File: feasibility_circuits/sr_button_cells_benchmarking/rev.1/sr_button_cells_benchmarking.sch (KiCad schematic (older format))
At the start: 48 parts, among them J1 Current Measurement, J10 Jumper, J11 EN_MED_CURR, J12 Jumper, J2 EN_POT, J3 GND, J4 GND, J5 Jumper, J6 VIN, J7 EN_HIGH_CURR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

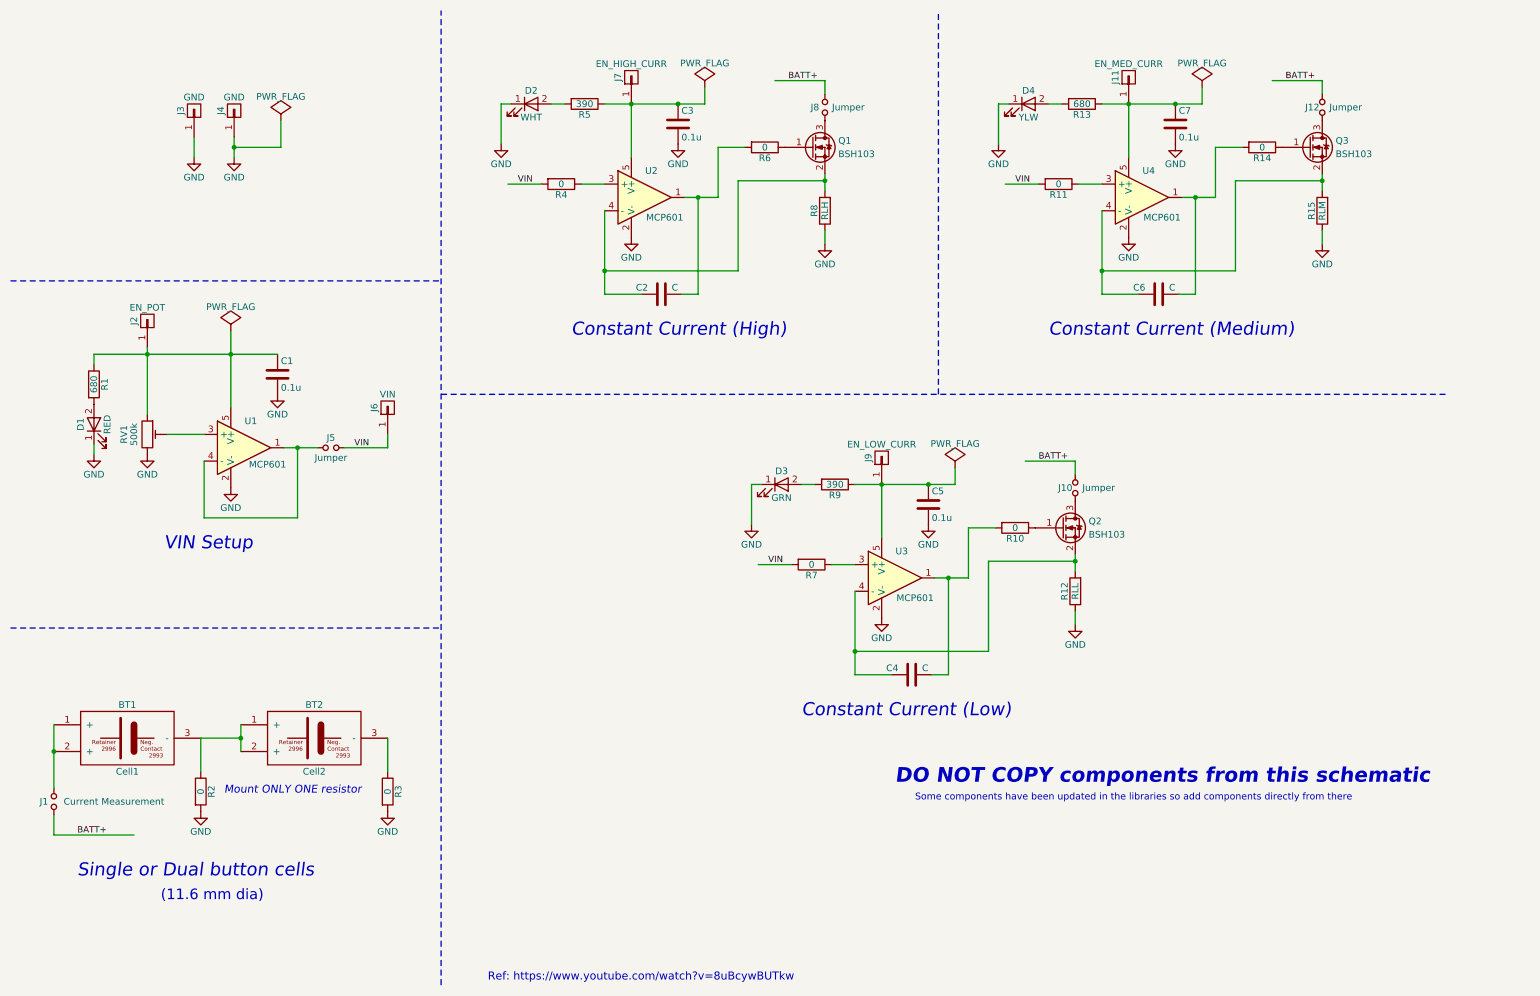
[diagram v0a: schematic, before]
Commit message: Review and organisation
Review of Auxiliary PIC and IR barrier setup board. Organisation of
resources.
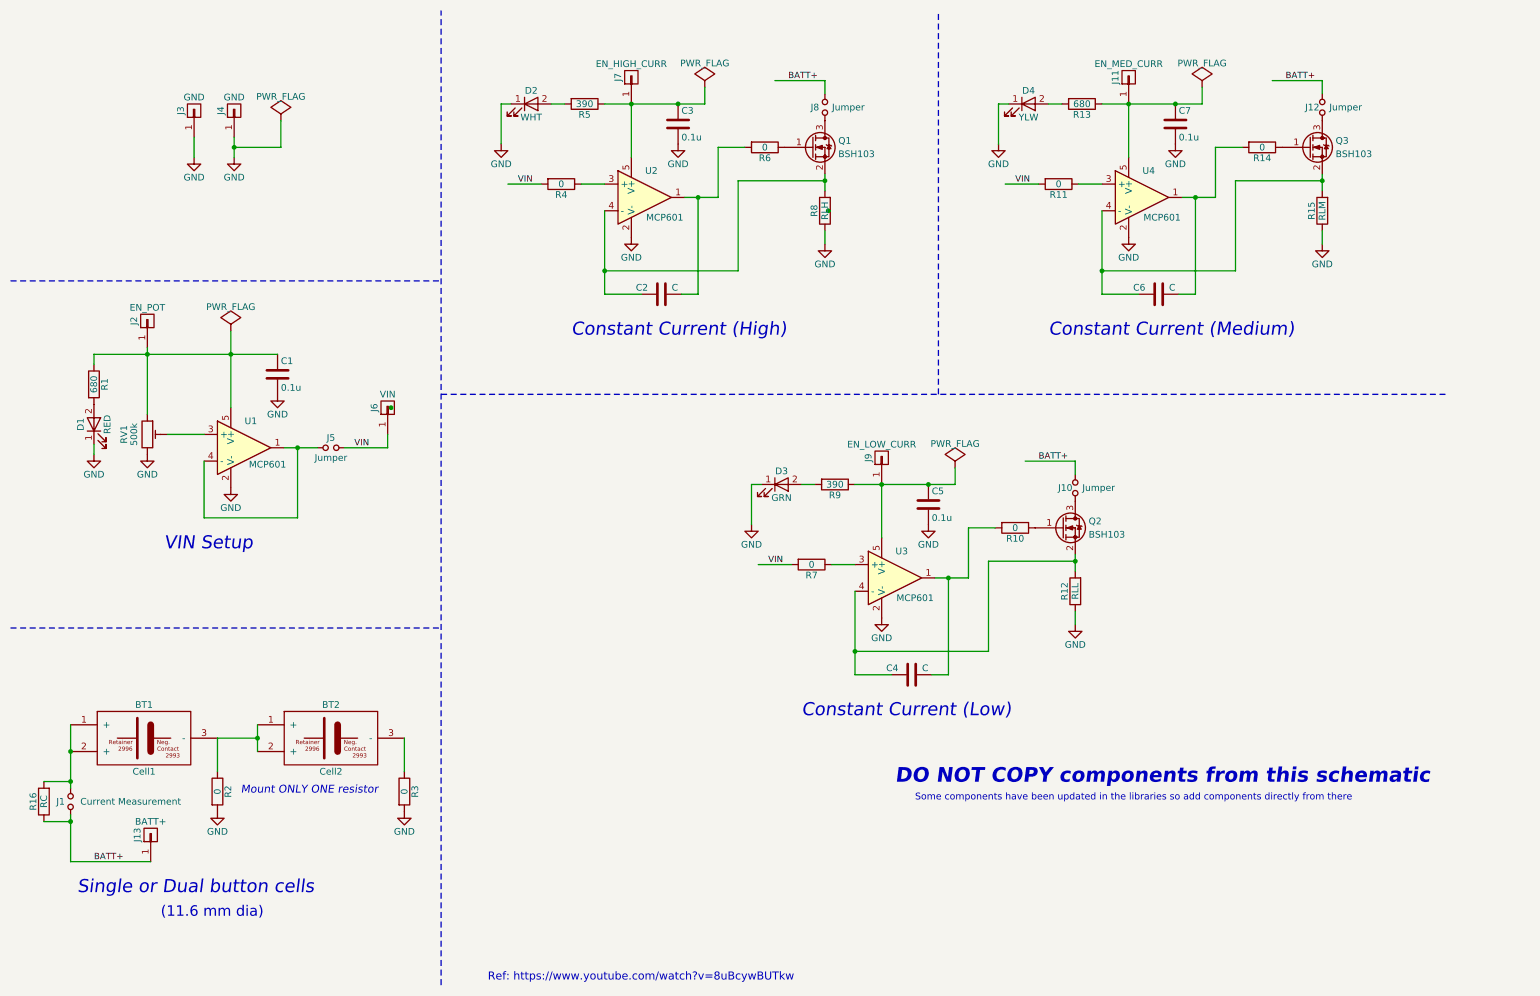
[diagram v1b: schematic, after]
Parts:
- added J13: BATT+, Custom_Connectors_SMD:proto_smd_pad-sq.-3mm, symbol CONN_01X01
- added R16: RC, Resistors_SMD:R_0805_HandSoldering, symbol R
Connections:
- wire segments 91 -> 92
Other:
- moved on the sheet: BT1, BT2, J1, R2, R3
